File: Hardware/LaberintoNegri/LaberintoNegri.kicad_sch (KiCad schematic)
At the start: 43 parts

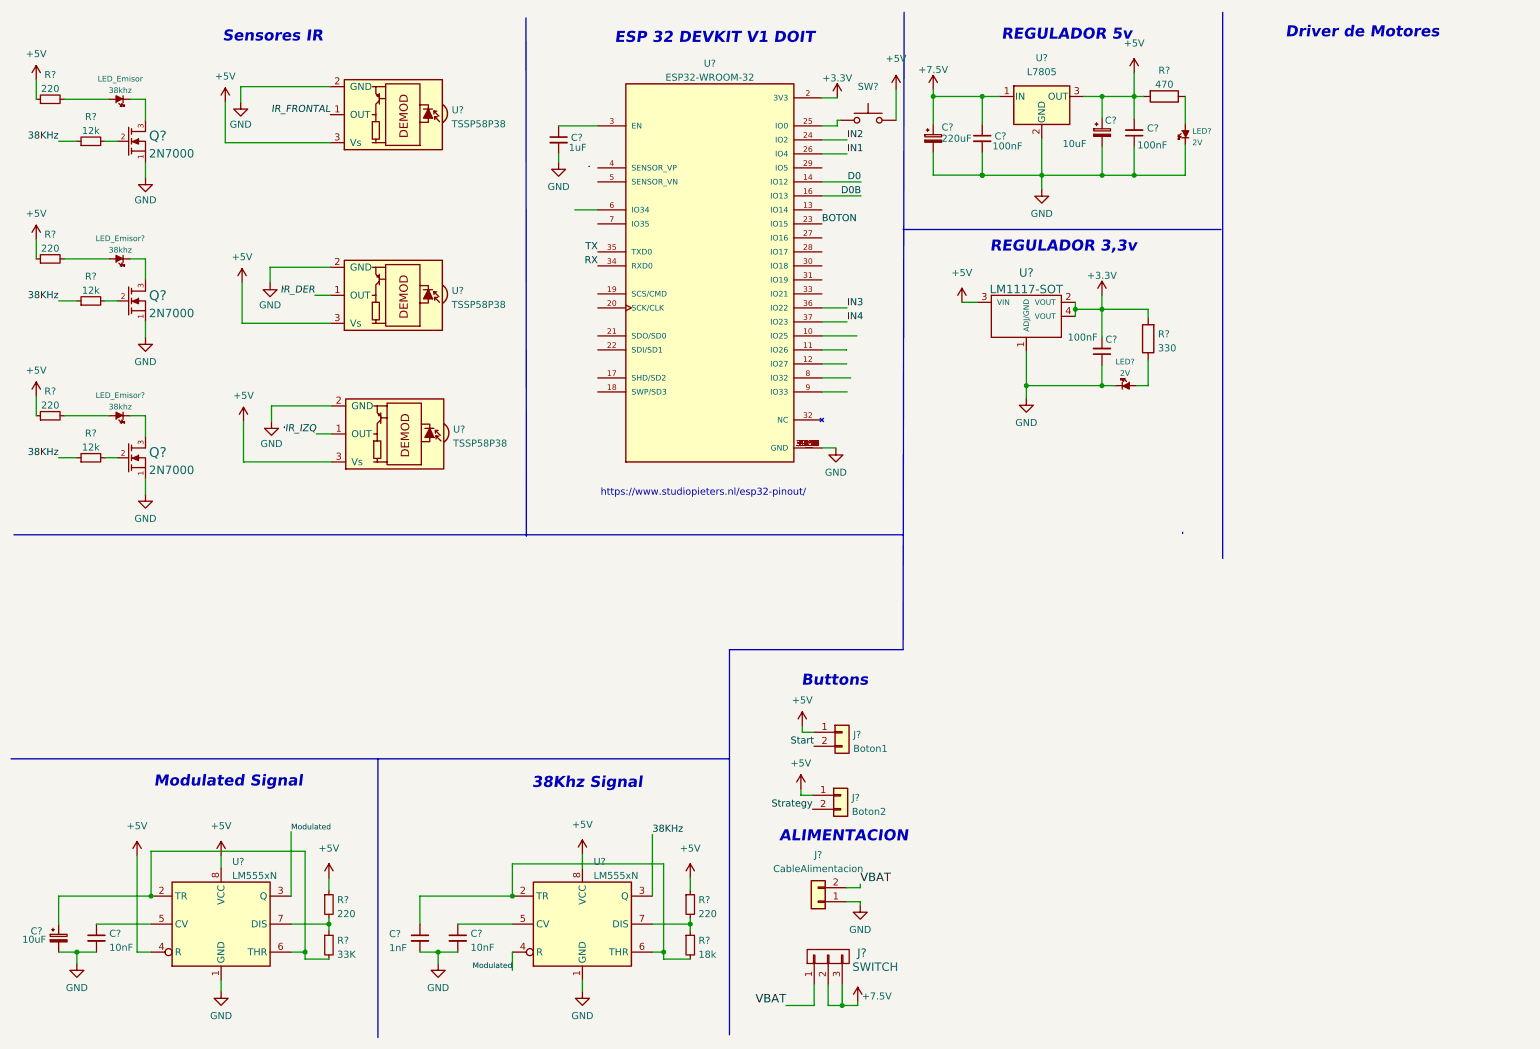
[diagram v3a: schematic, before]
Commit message: add drivers de motores , falta ordenar pines, y borre IR de la primera version prueba de Bover lo voy a hacer externamente y estoy viendo la pisibilidad de agregar el uart usb directo a la placa
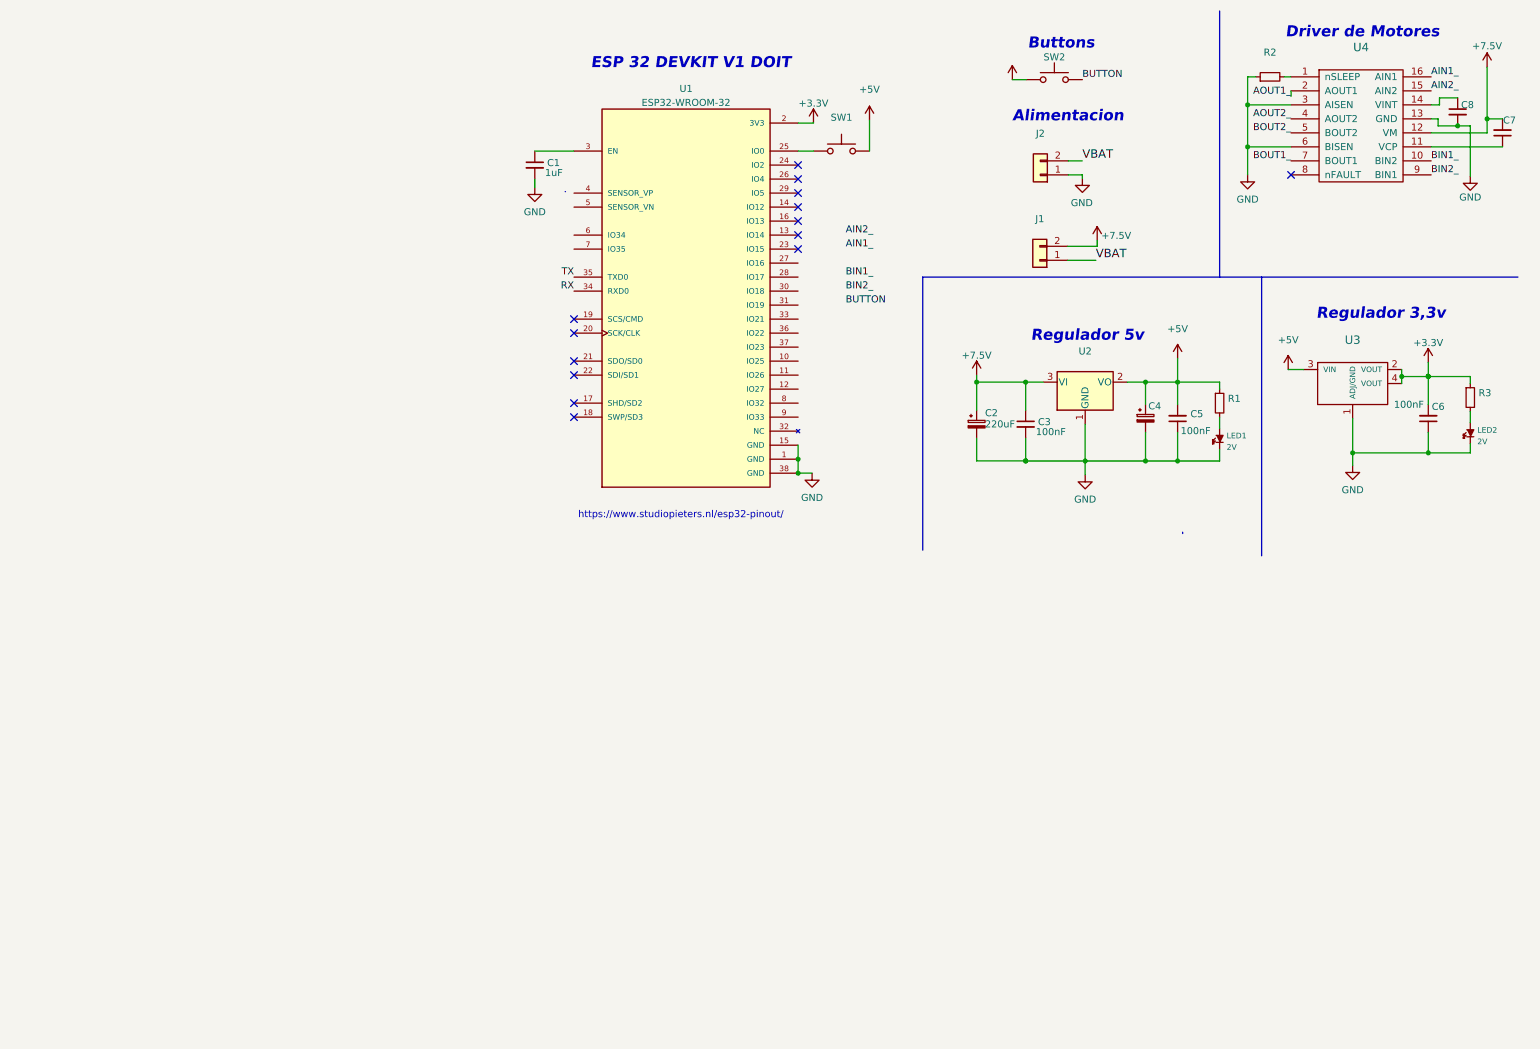
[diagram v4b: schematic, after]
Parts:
- removed C?: 10uF, symbol Device:C_Polarized_Small
- removed C? (x2): 10nF, symbol Device:C_Small
- removed C?: 1nF, symbol Device:C_Small
- removed J?: Boton2, Connector_PinSocket_2.54mm:PinSocket_1x02_P2.54mm_Vertical, symbol Connector_Generic:Conn_01x02
- removed J?: SWITCH, EESTN5:SW_SPDT_TH_Vertical, symbol EESTN5:Conn_01X03
- removed J?: Boton1, Connector_PinSocket_2.54mm:PinSocket_1x02_P2.54mm_Vertical, symbol Connector_Generic:Conn_01x02
- removed LED?: 2V, LED_SMD:LED_1206_3216Metric, symbol EESTN5:LED
- removed LED_Emisor, LED_Emisor? (x2): 38khz, symbol EESTN5:LED
- removed Q? (x3): 2N7000, EESTN5:SOT23, symbol EESTN5:2N7000
- removed R? (x5): 220, symbol Device:R_Small
- removed R?: 18k, symbol Device:R_Small
- removed R?: 470, EESTN5:R_1206, symbol Device:R
- removed R?: 33K, symbol Device:R_Small
- removed R? (x3): 12k, symbol Device:R_Small
- removed R?: 330, EESTN5:R_1206, symbol Device:R
- removed U? (x2): LM555xN, Package_DIP:DIP-8_W7.62mm, symbol Timer:LM555xN
- removed U?: L7805, EESTN5:to220, symbol Regulator_Linear:L7805
- removed U? (x3): TSSP58P38, OptoDevice:Vishay_MINICAST-3Pin, symbol Sensor_Proximity:TSSP58P38
- added C7, C8: (no value), symbol Device:C_Small
- added J1: (no value), Connector_PinHeader_2.54mm:PinHeader_1x02_P2.54mm_Vertical, symbol Connector_Generic:Conn_01x02
- added LED2: 2V, LED_SMD:LED_1206_3216Metric, symbol EESTN5:LED
- added R1, R2, R3: (no value), symbol Device:R_Small
- added SW2: (no value), symbol EESTN5:SW_Push
- added U2: (no value), symbol Regulator_Linear:LM1117-5.0
- added U4: (no value), symbol EESTN5:DRV8833
- C1, C3, C5, C6: renamed from C?; footprint Capacitor_SMD:C_1206_3216Metric -> (none)
- C4: renamed from C?; value 10uF -> (none)
- J2: renamed from J?; value CableAlimentacion -> (none)
- U3: renamed from U?; value LM1117-SOT -> (none)
- gave numbers to parts that had none: 4
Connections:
- net +3V3: now also R3.1, SW2.1
- net +5V: now also R1.1, U2.2 (VO)
- net +7.5V: now also C8.2, J1.2 (Pin_2), U2.3 (VI), U4.12 (VM)
- net GND: now also C7.2, LED2.2 (K), R2.1, U2.1 (GND), U4.13 (GND), U4.3 (AISEN), U4.6 (BISEN); no longer U1.39_1 (GND), U1.39_10 (GND), U1.39_11 (GND), U1.39_12 (GND), U1.39_13 (GND), U1.39_14 (GND), U1.39_15 (GND), U1.39_16 (GND), U1.39_17 (GND), U1.39_18 (GND), U1.39_19 (GND), U1.39_2 (GND), U1.39_20 (GND), U1.39_21 (GND), U1.39_3 (GND), U1.39_4 (GND), U1.39_5 (GND), U1.39_6 (GND), U1.39_7 (GND), U1.39_8 (GND), U1.39_9 (GND)
- net VBAT: now also J1.1 (Pin_1)
- net at LED1.1 (A): now also R1.2
- net BOTON: no longer names the net of U1.23 (IO15)
- net D0: no longer names the net of U1.14 (IO12)
- net D0B: no longer names the net of U1.16 (IO13)
- net IN1: no longer names the net of U1.26 (IO4)
- net IN2: no longer names the net of U1.24 (IO2)
- net IN3: no longer names the net of U1.36 (IO22)
- net IN4: no longer names the net of U1.37 (IO23)
- new net: C7.1, U4.14 (VINT)
- new net: LED2.1 (A), R3.2
- new net: C8.1, U4.11 (VCP)
- new net: R2.2, U4.1 (nSLEEP)
- new net AIN1_: U4.16 (AIN1)
- new net AIN2_: U4.15 (AIN2)
- new net AOUT1_: U4.2 (AOUT1)
- new net AOUT2_: U4.4 (AOUT2)
- new net BIN1_: U4.10 (BIN2)
- new net BIN2_: U4.9 (BIN1)
- new net BOUT1_: U4.7 (BOUT1)
- new net BOUT2_: U4.5 (BOUT2)
- new net BUTTON: SW2.2
- no-connect marks 0 -> 14
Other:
- note added: "Alimentacion"
- note added: "Regulador 3,3v"
- note added: "Regulador 5v"
- note removed: "38Khz Signal"
- note removed: "ALIMENTACION"
- note removed: "Modulated Signal"
- note removed: "REGULADOR 3,3v"
- note removed: "REGULADOR 5v"
- note removed: "Sensores IR"
- moved on the sheet: C1, C2, C3, C4, C5, C6, J2, LED1, SW1, U3

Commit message: emepzando con la conexiones uart/usb del esp32
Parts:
- added C?: 100nF, symbol Device:C_Small
- added C?: 1uF, symbol Device:C_Small
- added D?: D_Small, symbol Device:D_Small
- added D? (x2): D_Zener_Small, symbol Device:D_Zener_Small
- added J?: USB_B_Micro, symbol Connector:USB_B_Micro
- added U?: CP2102-GM, QFN50P500X500X100-29N, symbol CP2102:CP2102-GM
- C1, C3, C5: footprint (none) -> EESTN5:C_1206
- C4: value (none) -> 220uF
- C6: value 100nF -> (none); footprint (none) -> EESTN5:C_1206
- C7: value (none) -> 2,2uF; footprint (none) -> EESTN5:C_1206
- C8: value (none) -> 10nF; footprint (none) -> EESTN5:C_1206
- J1: value (none) -> Jumper
- J2: value (none) -> Battery
- R1: value (none) -> 470; footprint (none) -> EESTN5:R_1206
- R2: value (none) -> 47K; footprint (none) -> EESTN5:R_1206
- R3: value (none) -> 330; footprint (none) -> EESTN5:R_1206
- SW1: footprint (none) -> EESTN5:SW_PUSH-12mm
- SW2: value (none) -> SW_Push; footprint (none) -> EESTN5:SW_PUSH-12mm
- U2: value (none) -> LM1117-5.0; footprint (none) -> EESTN5:SOT223
- U3: value (none) -> LM1117 3.3v
- U4: value (none) -> DRV8833
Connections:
- net +3V3: no longer R3.1
- net +5V: now also R3.1
- net GND: now also C?.2, C?.2, D?.1 (K), D?.1 (K), J?.5 (GND), U?.29 (GND), U?.3 (GND)
- net TX renamed TXD
- net TXD: now also U?.26 (TXD)
- new net: D?.2 (A), J?.1 (VBUS)
- new net: C?.1, C?.1, U?.6 (VDD), U?.7 (REGIN), U?.8 (VBUS)
- new net +5VA: D?.1 (K)
- new net RXD: U?.25 (RXD)
- new net USB_D+: D?.2 (A), J?.3 (D+), U?.4 (D+)
- new net USB_D-: D?.2 (A), J?.2 (D-), U?.5 (D–)
- no-connect marks 14 -> 16
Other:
- moved on the sheet: C6, LED2, R3, U3
